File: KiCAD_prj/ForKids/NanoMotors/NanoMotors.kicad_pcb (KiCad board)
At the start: 2 copper layers, 112.2 x 52.9 mm, 27 parts, among them J1 Conn_01x15_Female, J10 M1, J2 Conn_01x15_Female, J3 Conn_01x15_Female, J4 Conn_01x15_Female, J5 Conn_01x15_Female, J6 Conn_01x15_Female, J7 Conn_01x02_Female, J8 Screw_Terminal_01x02, J9 M2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

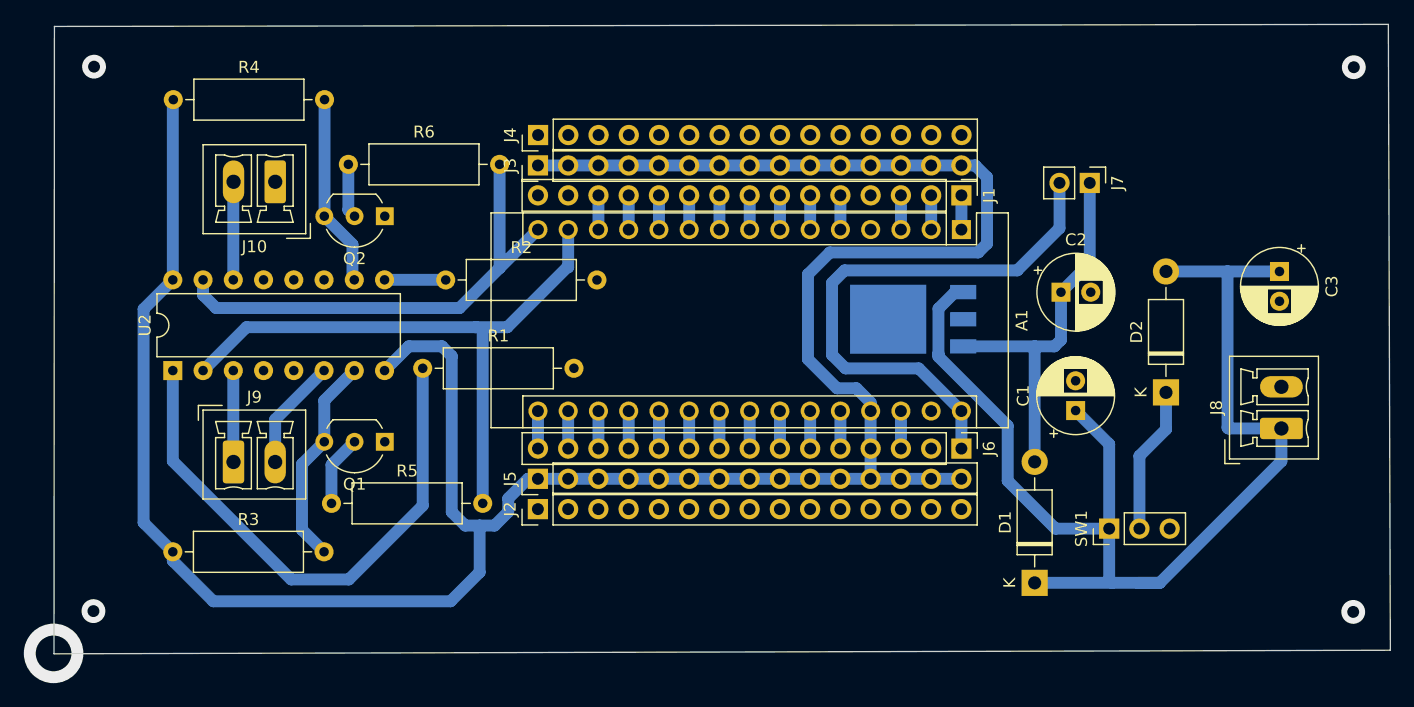
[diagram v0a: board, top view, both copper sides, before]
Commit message: Update ADB 2.1 end NanoMotors projects
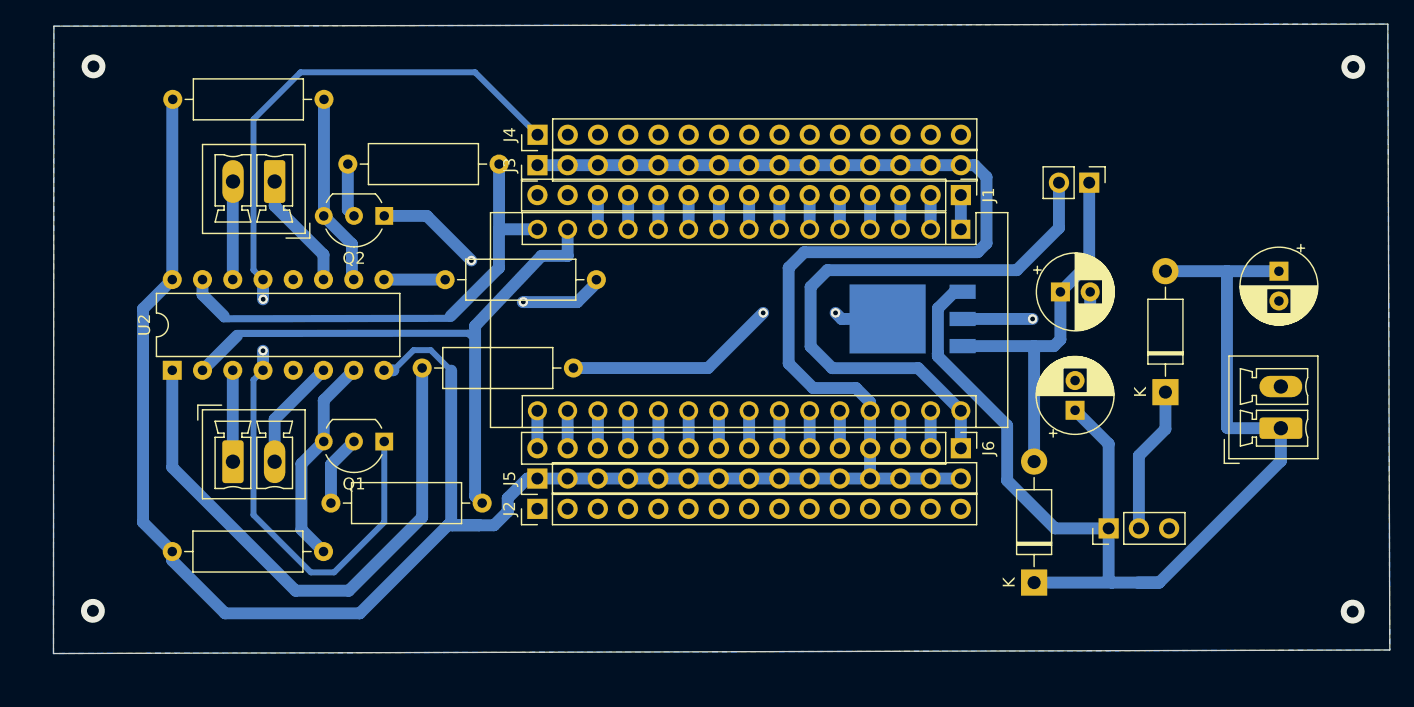
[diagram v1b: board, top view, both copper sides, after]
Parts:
- moved A1 0.05 mm to (76.2, -35.6)
- moved C2 0.05 mm to (84.6, -30.4)
- moved C3 0.05 mm to (102.9, -32.1)
- moved J7 0.05 mm to (87.0, -39.5)
- moved R6 0.05 mm to (24.7, -41.1)
- moved SW1 0.05 mm to (88.6, -10.5)
- moved D1 0.05 mm to (82.3, -5.95)
- moved R5 0.05 mm to (23.3, -12.6)
- moved C1 0.05 mm to (85.8, -20.4)
- moved D2 0.05 mm to (93.4, -21.9)
- moved J6 0.05 mm to (76.2, -17.2)
- moved J8 0.05 mm to (103.1, -18.9)
- moved J1 0.05 mm to (76.2, -38.5)
- moved J10 0.05 mm to (18.6, -39.6)
- moved J4 0.05 mm to (40.6, -43.6)
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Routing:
- net Earth: track 0.00 -> 131.4 mm, vias 0 -> 8
- net Net-(J10-Pad1): track 0.00 -> 9.93 mm
- net VIN: track 46.8 -> 49.7 mm
- net 5V: track 218.5 -> 220.3 mm
- net Net-(R1-Pad1): track 46.8 -> 48.5 mm
- net D12: track 41.3 -> 40.8 mm
- net (no net): vias 5 -> 4
- added copper zone on B.Cu, net Earth

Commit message: Update NanoMotors project: fix pcd board and update schem pdf file
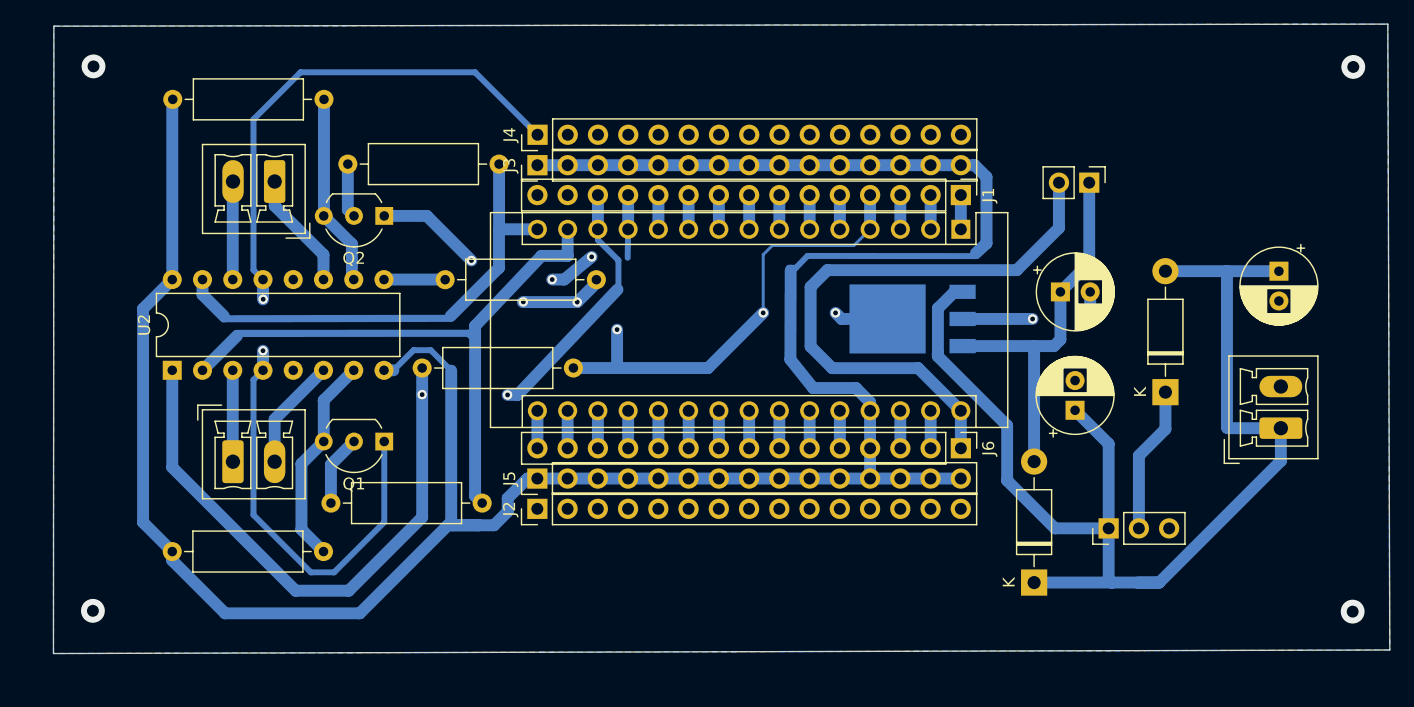
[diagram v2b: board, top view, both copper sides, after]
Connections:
- J1 pad 12: D9 -> Net-(J1-Pad12)
- J1 pad 13: D10 -> Net-(J1-Pad13)
- R1 pad 1: Net-(R1-Pad1) -> D10
- R2 pad 1: Net-(R2-Pad1) -> D9
- U2 pad 1: Net-(R1-Pad1) -> D10
- U2 pad 9: Net-(R2-Pad1) -> D9
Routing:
- net D10: track 2.88 -> 70.4 mm, vias 0 -> 2
- net Net-(R1-Pad1): track 48.5 -> 0.00 mm
- net Earth: track 131.4 -> 149.3 mm, vias 8 -> 10
- net D9: track 2.88 -> 14.4 mm, vias 0 -> 2
- net Net-(R2-Pad1): track 5.14 -> 0.00 mm
